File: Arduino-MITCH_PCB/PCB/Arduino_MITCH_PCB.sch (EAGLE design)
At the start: 12 parts, among them J1 1725656

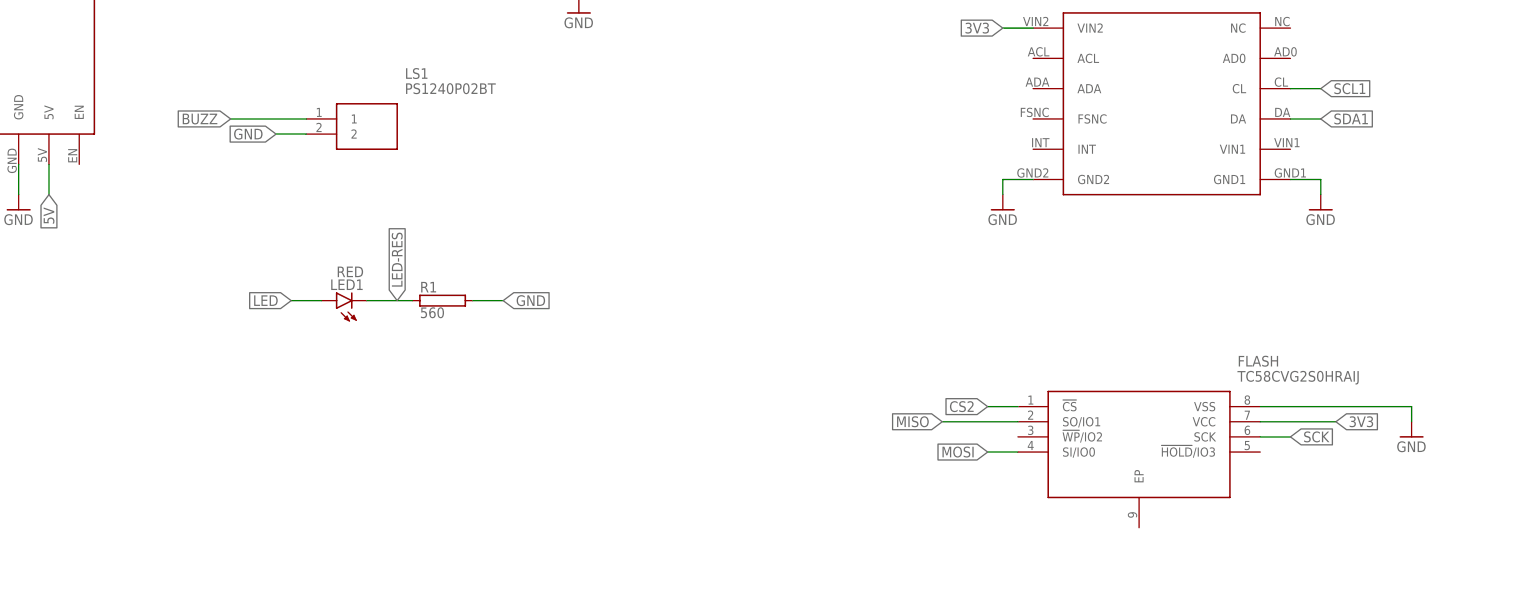
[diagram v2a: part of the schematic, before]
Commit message: Fixed Flash, added GND plane
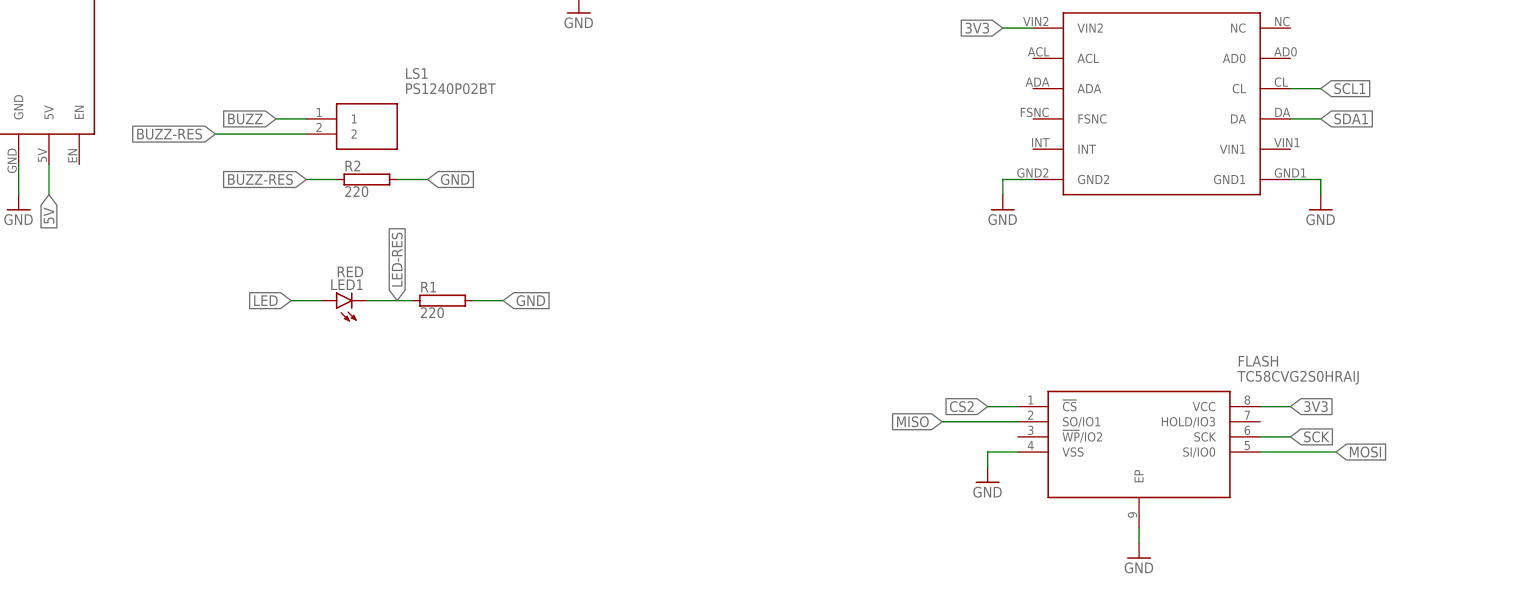
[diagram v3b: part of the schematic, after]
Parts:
- added R2: 220, resistor-power:RHPS58
- R1: value 560 -> 220
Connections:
- new net BUZZ-RES: LS1.2, R2.1
- net GND: now also FLASH.EP, R2.2; no longer LS1.2
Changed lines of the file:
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@@
 <part name="LS1" library="SamacSys_Parts" deviceset="PS1240P02BT" device=""/>
 <part name="LED1" library="led" library_urn="urn:adsk.eagle:library:259" deviceset="LED" device="5MM" package3d_urn="urn:adsk.eagle:package:15799/2" value="RED"/>
-<part name="R1" library="resistor-power" library_urn="urn:adsk.eagle:library:344" deviceset="R" device="HPS58" package3d_urn="urn:adsk.eagle:package:25160/1" value="560"/>
+<part name="R1" library="resistor-power" library_urn="urn:adsk.eagle:library:344" deviceset="R" device="HPS58" package3d_urn="urn:adsk.eagle:package:25160/1" value="220"/>
+<part name="GND15" library="supply1" library_urn="urn:adsk.eagle:library:371" deviceset="GND" device=""/>
+<part name="R2" library="resistor-power" library_urn="urn:adsk.eagle:library:344" deviceset="R" device="HPS58" package3d_urn="urn:adsk.eagle:package:25160/1" value="220"/>
 </parts>
 <sheets>
@@
 <attribute name="VALUE" x="99.06" y="7.62" size="1.778" layer="96"/>
 </instance>
-<instance part="GND14" gate="1" x="116.84" y="-27.94" smashed="yes">
-<attribute name="VALUE" x="114.3" y="-30.48" size="1.778" layer="96"/>
+<instance part="GND14" gate="1" x="45.72" y="-35.56" smashed="yes">
+<attribute name="VALUE" x="43.18" y="-38.1" size="1.778" layer="96"/>
 </instance>
 <instance part="LS1" gate="G$1" x="-68.58" y="25.4" smashed="yes">
@@
 <attribute name="NAME" x="-49.53" y="-3.7084" size="1.778" layer="95"/>
 <attribute name="VALUE" x="-49.53" y="-8.001" size="1.778" layer="96"/>
+</instance>
+<instance part="GND15" gate="1" x="71.12" y="-48.26" smashed="yes">
+<attribute name="VALUE" x="68.58" y="-50.8" size="1.778" layer="96"/>
+</instance>
+<instance part="R2" gate="G$1" x="-58.42" y="15.24" smashed="yes">
+<attribute name="NAME" x="-62.23" y="16.6116" size="1.778" layer="95"/>
+<attribute name="VALUE" x="-62.23" y="12.319" size="1.778" layer="96"/>
 </instance>
 </instances>
@@
 <segment>
 <pinref part="FLASH" gate="G$1" pin="VSS"/>
-<wire x1="91.44" y1="-22.86" x2="116.84" y2="-22.86" width="0.1524" layer="91"/>
-<wire x1="116.84" y1="-22.86" x2="116.84" y2="-25.4" width="0.1524" layer="91"/>
+<wire x1="50.8" y1="-30.48" x2="45.72" y2="-30.48" width="0.1524" layer="91"/>
+<wire x1="45.72" y1="-30.48" x2="45.72" y2="-33.02" width="0.1524" layer="91"/>
 <pinref part="GND14" gate="1" pin="GND"/>
-</segment>
-<segment>
-<pinref part="LS1" gate="G$1" pin="2"/>
-<wire x1="-68.58" y1="22.86" x2="-73.66" y2="22.86" width="0.1524" layer="91"/>
-<label x="-73.66" y="22.86" size="1.778" layer="95" rot="R180" xref="yes"/>
 </segment>
 <segment>
@@
 <wire x1="-40.64" y1="-5.08" x2="-35.56" y2="-5.08" width="0.1524" layer="91"/>
 <label x="-35.56" y="-5.08" size="1.778" layer="95" xref="yes"/>
+</segment>
+<segment>
+<pinref part="FLASH" gate="G$1" pin="EP"/>
+<wire x1="71.12" y1="-43.18" x2="71.12" y2="-45.72" width="0.1524" layer="91"/>
+<pinref part="GND15" gate="1" pin="GND"/>
+</segment>
+<segment>
+<pinref part="R2" gate="G$1" pin="2"/>
+<wire x1="-53.34" y1="15.24" x2="-48.26" y2="15.24" width="0.1524" layer="91"/>
+<label x="-48.26" y="15.24" size="1.778" layer="95" xref="yes"/>
 </segment>
 </net>
@@
 <segment>
 <pinref part="FLASH" gate="G$1" pin="VCC"/>
-<wire x1="91.44" y1="-25.4" x2="104.14" y2="-25.4" width="0.1524" layer="91"/>
-<label x="104.14" y="-25.4" size="1.778" layer="95" xref="yes"/>
+<wire x1="91.44" y1="-22.86" x2="96.52" y2="-22.86" width="0.1524" layer="91"/>
+<label x="96.52" y="-22.86" size="1.778" layer="95" xref="yes"/>
 </segment>
 </net>
@@
 <segment>
 <pinref part="FLASH" gate="G$1" pin="SI/IO0"/>
-<wire x1="50.8" y1="-30.48" x2="45.72" y2="-30.48" width="0.1524" layer="91"/>
-<label x="45.72" y="-30.48" size="1.778" layer="95" rot="R180" xref="yes"/>
+<wire x1="91.44" y1="-30.48" x2="104.14" y2="-30.48" width="0.1524" layer="91"/>
+<label x="104.14" y="-30.48" size="1.778" layer="95" xref="yes"/>
 </segment>
 </net>
@@
 <segment>
 <pinref part="LS1" gate="G$1" pin="1"/>
-<wire x1="-68.58" y1="25.4" x2="-81.28" y2="25.4" width="0.1524" layer="91"/>
-<label x="-81.28" y="25.4" size="1.778" layer="95" rot="R180" xref="yes"/>
+<wire x1="-68.58" y1="25.4" x2="-73.66" y2="25.4" width="0.1524" layer="91"/>
+<label x="-73.66" y="25.4" size="1.778" layer="95" rot="R180" xref="yes"/>
 </segment>
 <segment>
@@
 </segment>
 </net>
+<net name="BUZZ-RES" class="0">
+<segment>
+<pinref part="LS1" gate="G$1" pin="2"/>
+<wire x1="-68.58" y1="22.86" x2="-83.82" y2="22.86" width="0.1524" layer="91"/>
+<label x="-83.82" y="22.86" size="1.778" layer="95" rot="R180" xref="yes"/>
+</segment>
+<segment>
+<pinref part="R2" gate="G$1" pin="1"/>
+<wire x1="-63.5" y1="15.24" x2="-68.58" y2="15.24" width="0.1524" layer="91"/>
+<label x="-68.58" y="15.24" size="1.778" layer="95" rot="R180" xref="yes"/>
+</segment>
+</net>
